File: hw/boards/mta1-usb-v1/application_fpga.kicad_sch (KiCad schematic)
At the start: 38 parts, among them U10 PT2043AT6, U6 ICE40UP5K-SG48ITR, U8 W25Q80DVUXIE

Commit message: Add extended values, manufacturer/distributor info to components in mta1
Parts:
- C16, C17, C18, C19, C20, C21, C22, C23, C26: value 0.10uF -> (none); footprint mta1:CAPC1005X06L -> (none); Extended Value (none) -> 16V,X5R,20%; Manufacturer (none) -> Any/not critical
- C25: value 10uF -> (none); footprint mta1:CAPC1608X09L -> (none); Extended Value (none) -> 10V,X5R,20%; Manufacturer (none) -> Any/not critical
- C27: value 3pF -> (none); footprint mta1:CAPC1005X06L -> (none); Extended Value (none) -> 16V,X5R,20%; Manufacturer (none) -> Any/not critical
- C8: value 10uF 16V -> (none); footprint Capacitor_SMD:C_1206_3216Metric -> (none); Extended Value (none) -> 16V
- D3: value LED_ARGB -> (none); footprint mta1:0402rgb-1010 -> (none); Manufacturer (none) -> Foshan NationStar; Manufacturer Part Number (none) -> FC-B1010RGBT-HG; Supplier (none) -> LCSC; Supplier Part Number (none) -> C158099
- FB3: value BLM18KG300TN1D -> (none); footprint mta1:Ferritbead_0603_1608Metric -> (none); Manufacturer (none) -> Murata; Manufacturer Part Number (none) -> BLM18KG300TN1D; Supplier (none) -> Digikey; Supplier Part Number (none) -> 490-5447-1-ND
- R16, R17, R18: value 1K -> (none); footprint mta1:ERJ2G(0402)_L -> (none); Extended Value (none) -> 1/16W,5%; Manufacturer (none) -> Any/not critical
- R19, R20, R23, R24, R25, R26: value 10k -> (none); footprint mta1:ERJ2G(0402)_L -> (none); Extended Value (none) -> 1/16W,5%; Manufacturer (none) -> Any/not critical
- R30: value 2K -> (none); footprint mta1:ERJ2G(0402)_L -> (none); Extended Value (none) -> 1/16W,1%; Manufacturer (none) -> Any/not critical
- TP12: value APP_ICE_SCK -> (none); footprint TestPoint:TestPoint_Pad_D1.0mm -> (none); now left out of the parts list
- TP13: value APP_ICE_SS -> (none); footprint TestPoint:TestPoint_Pad_D1.0mm -> (none); now left out of the parts list
- TP14: value APP_ICE_MOSI -> (none); footprint TestPoint:TestPoint_Pad_D1.0mm -> (none); now left out of the parts list
- TP15: value APP_ICE_MISO -> (none); footprint TestPoint:TestPoint_Pad_D1.0mm -> (none); now left out of the parts list
- TP16: value APP_CRESET -> (none); footprint TestPoint:TestPoint_Pad_D1.0mm -> (none); now left out of the parts list
- TP17: value APP_CDONE -> (none); footprint TestPoint:TestPoint_Pad_D1.0mm -> (none); now left out of the parts list
- TP18: value APP_GPIO1 -> (none); footprint TestPoint:TestPoint_Pad_D1.0mm -> (none); now left out of the parts list
- TP19: value APP_GPIO2 -> (none); footprint TestPoint:TestPoint_Pad_D1.0mm -> (none); now left out of the parts list
- TP20: value APP_GPIO3 -> (none); footprint TestPoint:TestPoint_Pad_D1.0mm -> (none); now left out of the parts list
- TP21: value APP_GPIO4 -> (none); footprint TestPoint:TestPoint_Pad_D1.0mm -> (none); now left out of the parts list
- TP5: value APP_GND -> (none); footprint TestPoint:TestPoint_Pad_D1.0mm -> (none); now left out of the parts list
- U10: value PT2043AT6 -> (none); footprint Package_TO_SOT_SMD:SOT-23-6 -> (none); Manufacturer (none) -> PinTeng; Manufacturer Part Number (none) -> PT2043AT6; Supplier (none) -> LCSC; Supplier Part Number (none) -> C2914233
- U6: value ICE40UP5K-SG48ITR -> (none); footprint Package_DFN_QFN:QFN-48-1EP_7x7mm_P0.5mm_EP5.6x5.6mm -> (none); Manufacturer (none) -> Lattice; Manufacturer Part Number (none) -> ICE40UP5K-SG48ITR; Supplier (none) -> Digikey; Supplier Part Number (none) -> 220-2145-2-ND
- U8: value W25Q80DVUXIE -> (none); footprint mta1:W25Q80DVUXIE -> (none); Manufacturer (none) -> XTX; Manufacturer Part Number (none) -> XT25F08BDFIGT-S; Supplier (none) -> LCSC; Supplier Part Number (none) -> C558860

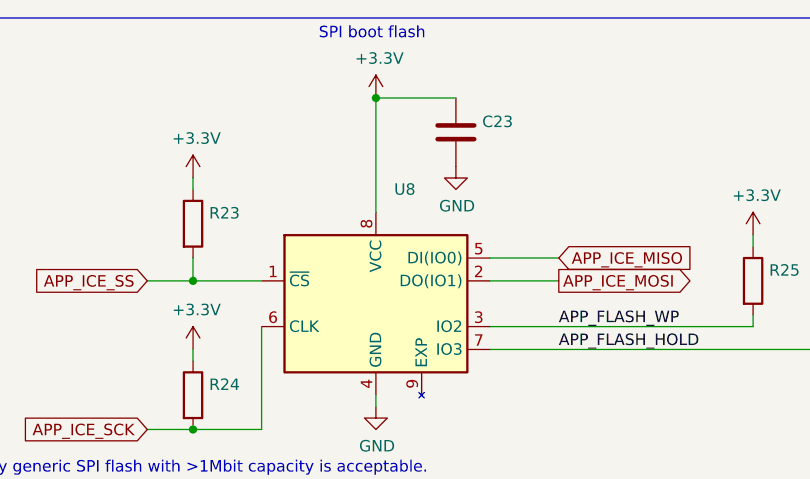
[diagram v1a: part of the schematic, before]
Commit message: Update MTA1-USB-V1 release files to match production
* Change SPI flash memory type to XT25F08BDFIGT-S
* Change touch sensor feedback cap to 1uF
* Add manufacturer, manufacturer part number, distributor, distributor part number
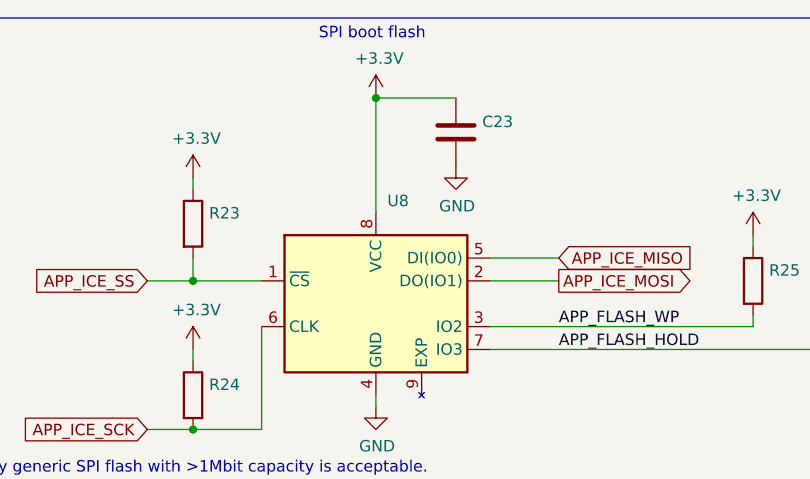
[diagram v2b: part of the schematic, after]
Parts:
- C8: Extended Value 16V -> 16V,X5R,10%; Manufacturer (none) -> Fenghua; Manufacturer Part Number (none) -> 1206X106K160NT; Supplier (none) -> LCSC; Supplier Part Number (none) -> C105478
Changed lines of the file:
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@@
     (in_bom yes) (on_board yes)
     (property "Reference" "C8" (id 0) (at 182.88 90.17 0))
-    (property "Value" "" (id 1) (at 186.69 92.71 0))
+    (property "Value" "" (id 1) (at 184.15 92.71 0))
     (property "Footprint" "" (id 2) (at 178.1048 87.63 0)
       (effects (font (size 1.27 1.27)) hide)
@@
       (effects (font (size 1.27 1.27)) hide)
     )
-    (property "Extended Value" "16V" (id 4) (at 179.07 91.44 0)
+    (property "Extended Value" "16V,X5R,10%" (id 4) (at 179.07 91.44 0)
+      (effects (font (size 1.27 1.27)) hide)
+    )
+    (property "Manufacturer" "Fenghua" (id 5) (at 179.07 91.44 0)
+      (effects (font (size 1.27 1.27)) hide)
+    )
+    (property "Manufacturer Part Number" "1206X106K160NT" (id 6) (at 179.07 91.44 0)
+      (effects (font (size 1.27 1.27)) hide)
+    )
+    (property "Supplier" "LCSC" (id 7) (at 179.07 91.44 0)
+      (effects (font (size 1.27 1.27)) hide)
+    )
+    (property "Supplier Part Number" "C105478" (id 8) (at 179.07 91.44 0)
       (effects (font (size 1.27 1.27)) hide)
     )
@@
   )
   (symbol (lib_id "mta1:W25Q80DVUXIE") (at 223.52 46.99 0) (unit 1)
-    (in_bom yes) (on_board yes) (fields_autoplaced)
-    (property "Reference" "U8" (id 0) (at 225.5394 34.29 0)
-      (effects (font (size 1.27 1.27)) (justify left))
-    )
-    (property "Value" "" (id 1) (at 225.5394 36.83 0)
-      (effects (font (size 1.27 1.27)) (justify left))
-    )
+    (in_bom yes) (on_board yes)
+    (property "Reference" "U8" (id 0) (at 224.79 35.56 0)
+      (effects (font (size 1.27 1.27)) (justify left))
+    )
+    (property "Value" "" (id 1) (at 224.79 38.1 0)
+      (effects (font (size 1.27 1.27)) (justify left))
+    )
